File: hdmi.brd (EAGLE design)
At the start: 160 x 100 mm, 151 parts, among them IC1 FT2232HQ, U0 6SLX45CSG324, U1 MT41J64M16, U2 TPD12S016RKTR, U3 TPD12S016RKTR, U4 TPD12S016RKTR, U5 MNR18, U6 MNR18, U8 20Mhz

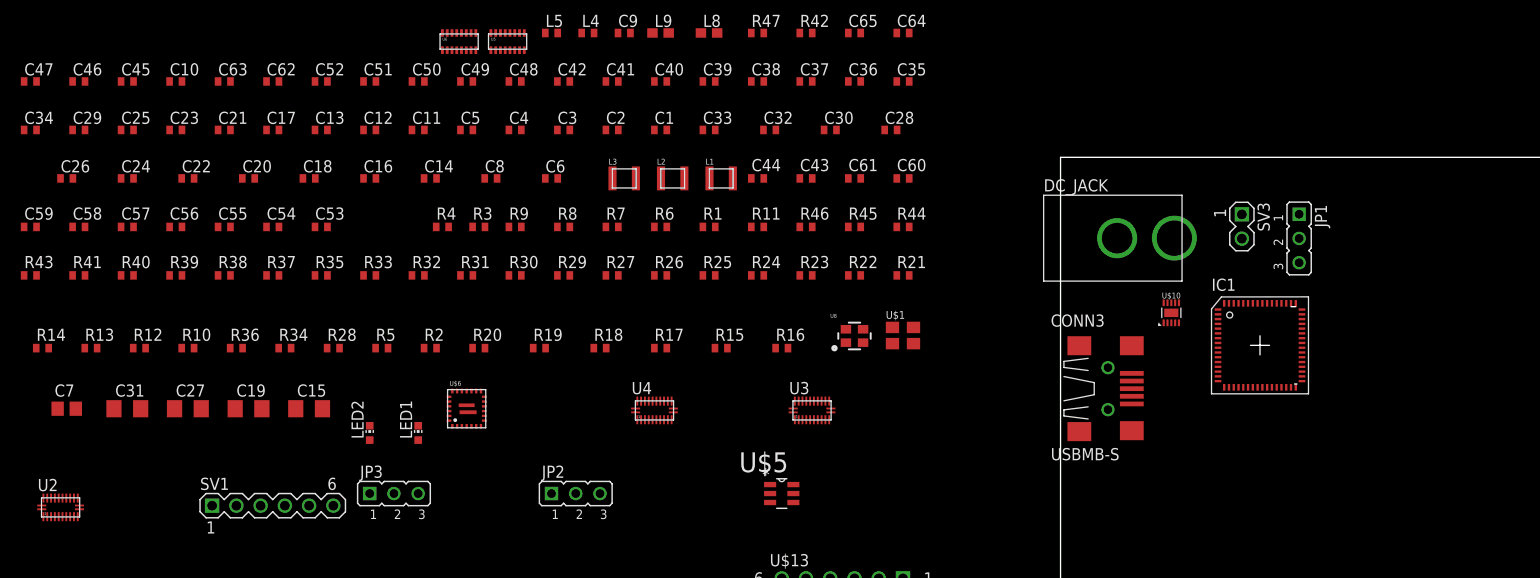
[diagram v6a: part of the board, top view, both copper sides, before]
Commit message: +First layout of power management
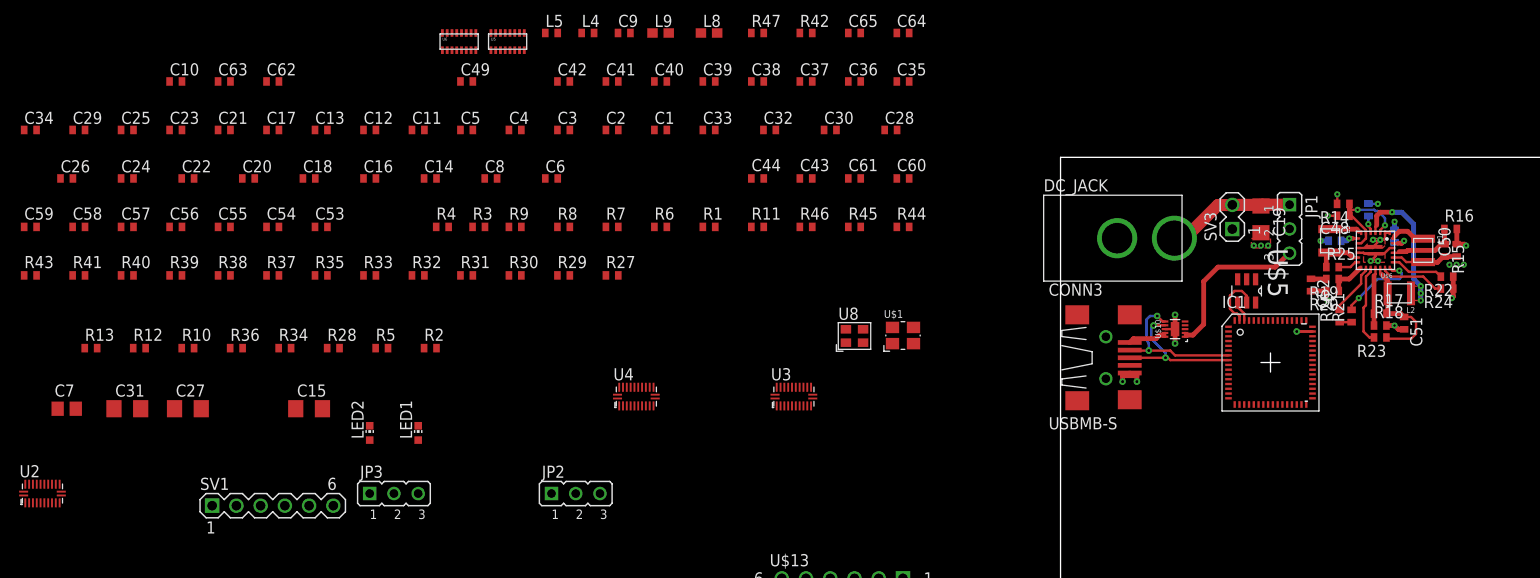
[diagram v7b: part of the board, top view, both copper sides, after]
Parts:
- moved C47 143.9 mm to (35.0, 91.8), flipped to the bottom, turned to 270 degrees
- moved R14 137.1 mm to (29.6, 95.1), turned to 180 degrees
- moved C46 132.7 mm to (28.8, 91.2), flipped to the bottom
- moved C45 130.7 mm to (32.2, 94.5), flipped to the bottom, turned to 90 degrees
- moved C51 111.3 mm to (36.0, 82.6), turned to 270 degrees
- moved C50 110.2 mm to (41.5, 90.2), turned to 90 degrees
- moved C19 107.9 mm to (21.0, 93.5), turned to 270 degrees
- moved C52 105.9 mm to (26.2, 86.6), turned to 270 degrees
- moved U$6 96.7 mm to (33.0, 90.2), turned to 180 degrees
- moved R20 89.7 mm to (28.5, 86.0), turned to 180 degrees
- moved C48 87.9 mm to (29.6, 93.9), turned to 180 degrees
- moved R19 83.4 mm to (28.5, 87.2), turned to 180 degrees
- moved R18 81.8 mm to (33.5, 82.4)
- moved L2 77.1 mm to (35.5, 85.8), turned to 180 degrees
- moved R15 76.5 mm to (40.2, 90.2), turned to 270 degrees
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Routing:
- net GND: track 0.00 -> 32.4 mm, vias 0 -> 18
- net USB_VBUS: track 0.00 -> 17.6 mm
- net N$7: track 0.00 -> 16.2 mm, vias 0 -> 2
- net N$8: track 0.00 -> 15.8 mm, vias 0 -> 2
- net N$16: track 0.00 -> 14.7 mm, vias 0 -> 4
- net CENTER: track 0.00 -> 13.6 mm
- net +1V5: track 0.00 -> 13.2 mm
- net N$15: track 0.00 -> 11.3 mm, vias 0 -> 2
- net +5V: track 0.00 -> 10.8 mm, vias 0 -> 6
- net N$22: track 0.00 -> 8.81 mm, vias 0 -> 2
- net +3V3: track 0.00 -> 8.36 mm, vias 0 -> 3
- net N$20: track 0.00 -> 8.32 mm
- net N$21: track 0.00 -> 7.38 mm
- net N$24: track 0.00 -> 6.90 mm
- net +1V2: track 0.00 -> 6.42 mm
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- added copper zone on layer 15, net +3V3
- added copper zone on layer 15, net +5V
- added copper zone on layer 1, net GND
- added copper zone on layer 2, net GND
- added copper zone on layer 1, net N$16

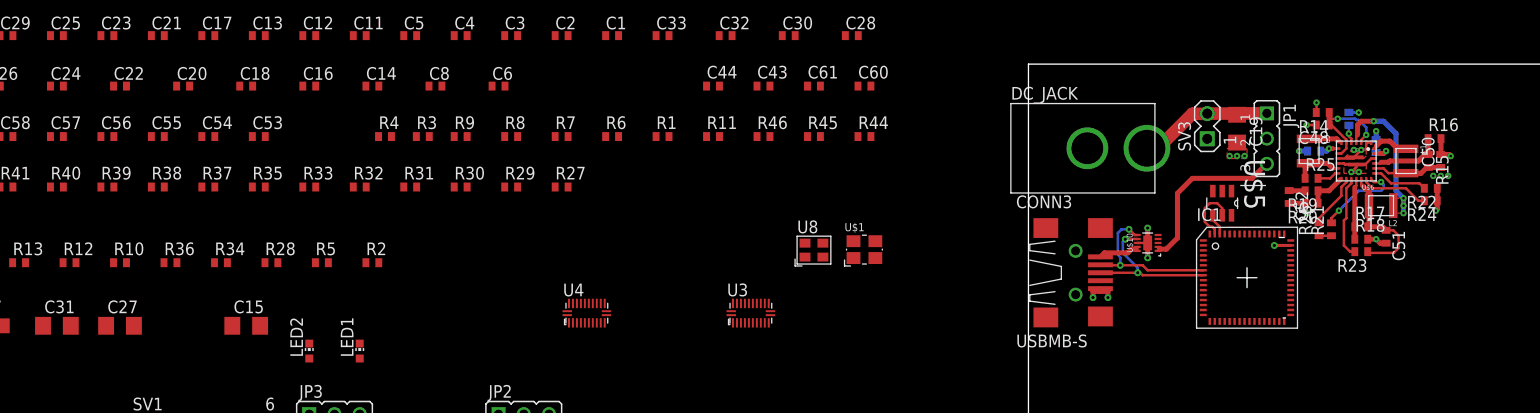
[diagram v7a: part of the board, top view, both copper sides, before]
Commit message: Moved bypass capacitors at the power management to the top layer
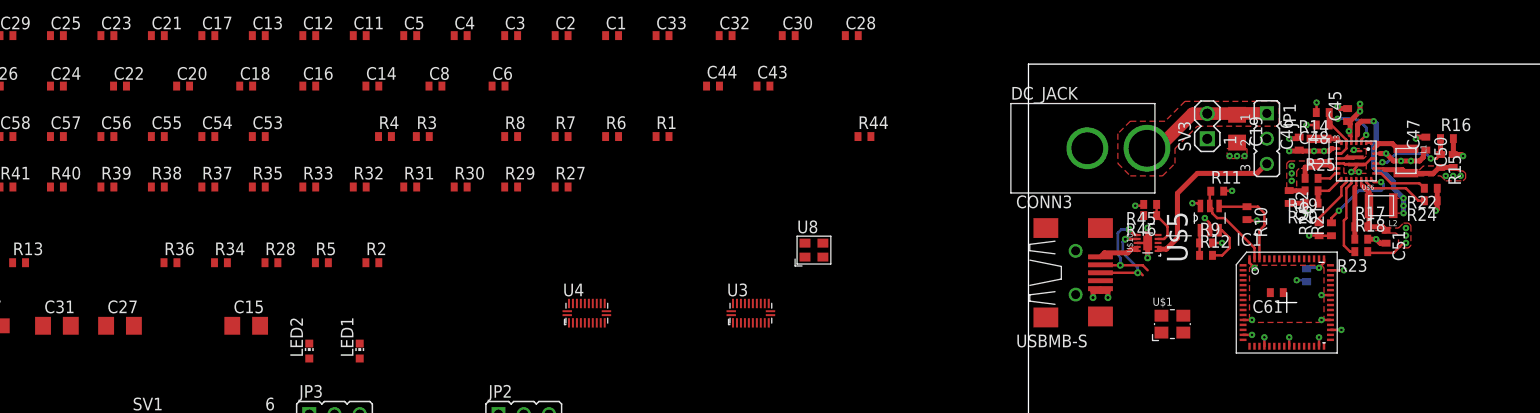
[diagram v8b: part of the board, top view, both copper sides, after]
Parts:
- moved R12 114.4 mm to (17.9, 80.8)
- moved R10 113.5 mm to (22.0, 85.0), turned to 270 degrees
- moved R9 75.8 mm to (17.9, 82.0)
- moved R11 51.0 mm to (19.0, 87.2)
- moved C61 51.0 mm to (25.0, 77.0), turned to 180 degrees
- moved C60 48.4 mm to (28.0, 78.8), flipped to the bottom, turned to 270 degrees
- moved R46 39.7 mm to (12.2, 84.8), turned to 180 degrees
- moved R45 34.5 mm to (12.2, 85.9), turned to 180 degrees
- moved U$1 31.9 mm to (14.5, 73.8)
- moved C47 5.01 mm to (40.0, 92.0), flipped to the top, turned to 90 degrees
- moved IC1 4.72 mm to (26.0, 76.0)
- moved U$5 1.95 mm to (18.2, 84.5), turned to 90 degrees
- moved C46 1.68 mm to (27.2, 92.0), flipped to the top, turned to 90 degrees
- moved C50 1.25 mm to (42.8, 90.2)
- moved R15 1.25 mm to (41.5, 90.2)
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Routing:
- net +3V3: track 8.36 -> 18.4 mm, vias 3 -> 12
- net +5V: track 10.8 -> 20.5 mm, vias 6 -> 11
- net N$9: track 2.17 -> 9.67 mm
- net N$8: track 15.8 -> 9.66 mm
- net N$7: track 16.2 -> 10.6 mm
- net +1V8: track 0.00 -> 5.31 mm, vias 0 -> 4
- net USB_5V_ACK#: track 0.00 -> 4.68 mm
- net N$10: track 0.00 -> 4.42 mm
- net GND: track 32.4 -> 36.7 mm, vias 18 -> 23
- net N$6: track 6.04 -> 9.15 mm
- net N$12: track 0.00 -> 2.57 mm
- net +1V2: track 6.42 -> 8.52 mm, vias 0 -> 3
- net +1V5: track 13.2 -> 11.5 mm, vias 0 -> 3
- net N$21: track 7.38 -> 9.05 mm, vias 0 -> 2
- net N$17: track 3.41 -> 2.41 mm
- added copper zone on layer 1, net +1V2
- added copper zone on layer 1, net +1V5
- added copper zone on layer 1, net +1V8
- added copper zone on layer 1, net +3V3
- added copper zone on layer 1, net CENTER
